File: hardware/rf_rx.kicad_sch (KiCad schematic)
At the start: 31 parts, among them J4 CON-SMA-EDGE-S, Q1 BC847C,215, U6 TL974IDR, U7 MAX4003

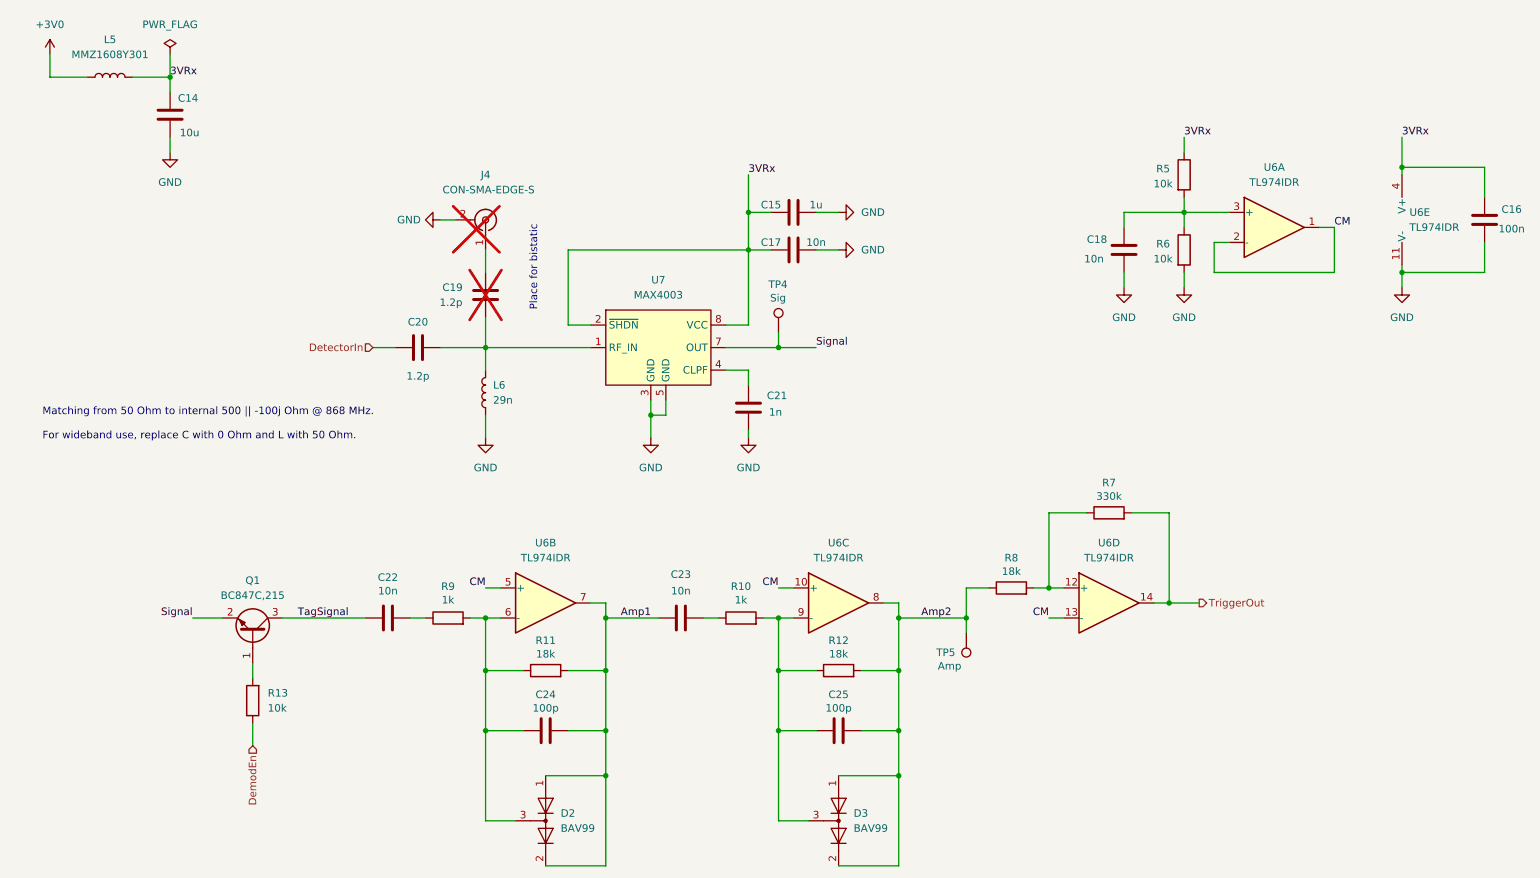
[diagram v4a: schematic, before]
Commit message: Rev 3. Back to transistor-based design since op-amp approach did not work well. Using UART bridge from other brand as FTDI was sold out.
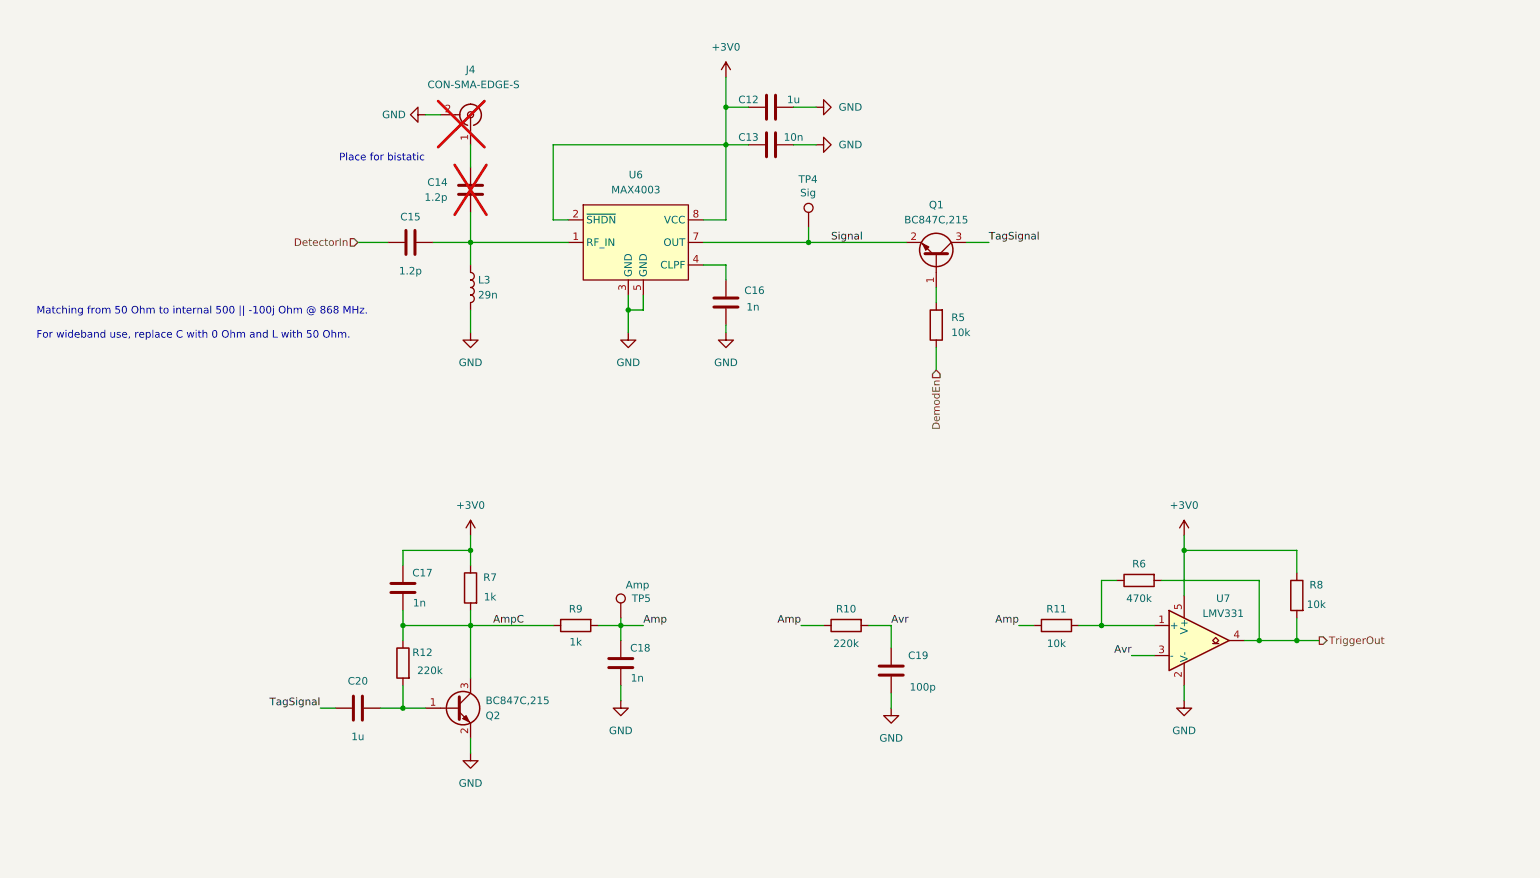
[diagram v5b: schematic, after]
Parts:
- removed C14: 10u, Capacitor_SMD:C_0603_1608Metric, symbol Device:C
- removed C16: 100n, Capacitor_SMD:C_0603_1608Metric, symbol Device:C
- removed C22, C23: 10n, Capacitor_SMD:C_0603_1608Metric, symbol Device:C
- removed C24, C25: 100p, Capacitor_SMD:C_0603_1608Metric, symbol Device:C
- removed D2, D3: BAV99, Package_TO_SOT_SMD:SOT-323_SC-70, symbol Diode:BAV99
- removed L5: MMZ1608Y301, Inductor_SMD:L_0603_1608Metric, symbol Device:L
- removed L6: 29n, Inductor_SMD:L_0603_1608Metric, symbol Device:L
- removed R5: 10k, Resistor_SMD:R_0603_1608Metric, symbol Device:R
- removed U6: TL974IDR, Package_SO:TSSOP-14_4.4x5mm_P0.65mm, symbol Amplifier_Operational:LM324
- added C17: 1n, Capacitor_SMD:C_0603_1608Metric, symbol Device:C
- added C19: 100p, Capacitor_SMD:C_0603_1608Metric, symbol Device:C
- added C20: 1u, Capacitor_SMD:C_0603_1608Metric, symbol Device:C
- added L3: 29n, Inductor_SMD:L_0603_1608Metric, symbol Device:L
- added Q2: BC847C,215, Package_TO_SOT_SMD:SOT-23, symbol Transistor_BJT:BC847
- added U7: LMV331, Package_TO_SOT_SMD:SOT-353_SC-70-5, symbol Comparator:LMV331
- C18: value 10n -> 1n
- R10: value 1k -> 220k
- R11, R8: value 18k -> 10k
- R12: value 18k -> 220k
- R6: value 10k -> 470k
- R7: value 330k -> 1k
- renumbered C15 to C12, C17 to C13, C19 to C14, C20 to C15, C21 to C16, R13 to R5, U7 to U6
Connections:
- net 3VRx is gone; now on net +3V0: C12.2, C13.2, U6.2 (~{SHDN}), U6.8 (VCC)
- net Amp1 is gone; now on an unnamed net: R11.2
- net +3V0: now also R7.1, R8.1, C17.1, U7.5 (V+)
- net GND: now also C18.2, C19.2, L3.2, Q2.2 (E), U7.2 (V-); no longer C18.1, R6.2
- net TagSignal: now also C20.1
- net TriggerOut: now also R6.2, R8.2, U7.4; no longer R7.2
- net Amp: now reaches R11.1, R9.2
- net Amp: now also C18.1, R10.1, TP5.1
- net AmpC: now reaches R12.1
- net AmpC: now also R7.2, R9.1, C17.2, Q2.3 (C); no longer R10.2
- net at R6.1: now also U7.1 (+); no longer C18.2
- net at C14.2, C15.1, U6.1 (RF_IN): now also L3.1
- removed net Amp2: R12.2, R8.1, TP5.1
- new net: C20.2, Q2.1 (B), R12.2
- new net Avr: C19.1, R10.2, U7.3 (-)
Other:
- moved on the sheet: C12, C13, C14, C15, C16, J4, Q1, R5, TP4, TP5, U6

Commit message: Rev 4. Removed coupler and detector IC. Using simple diode as detector.
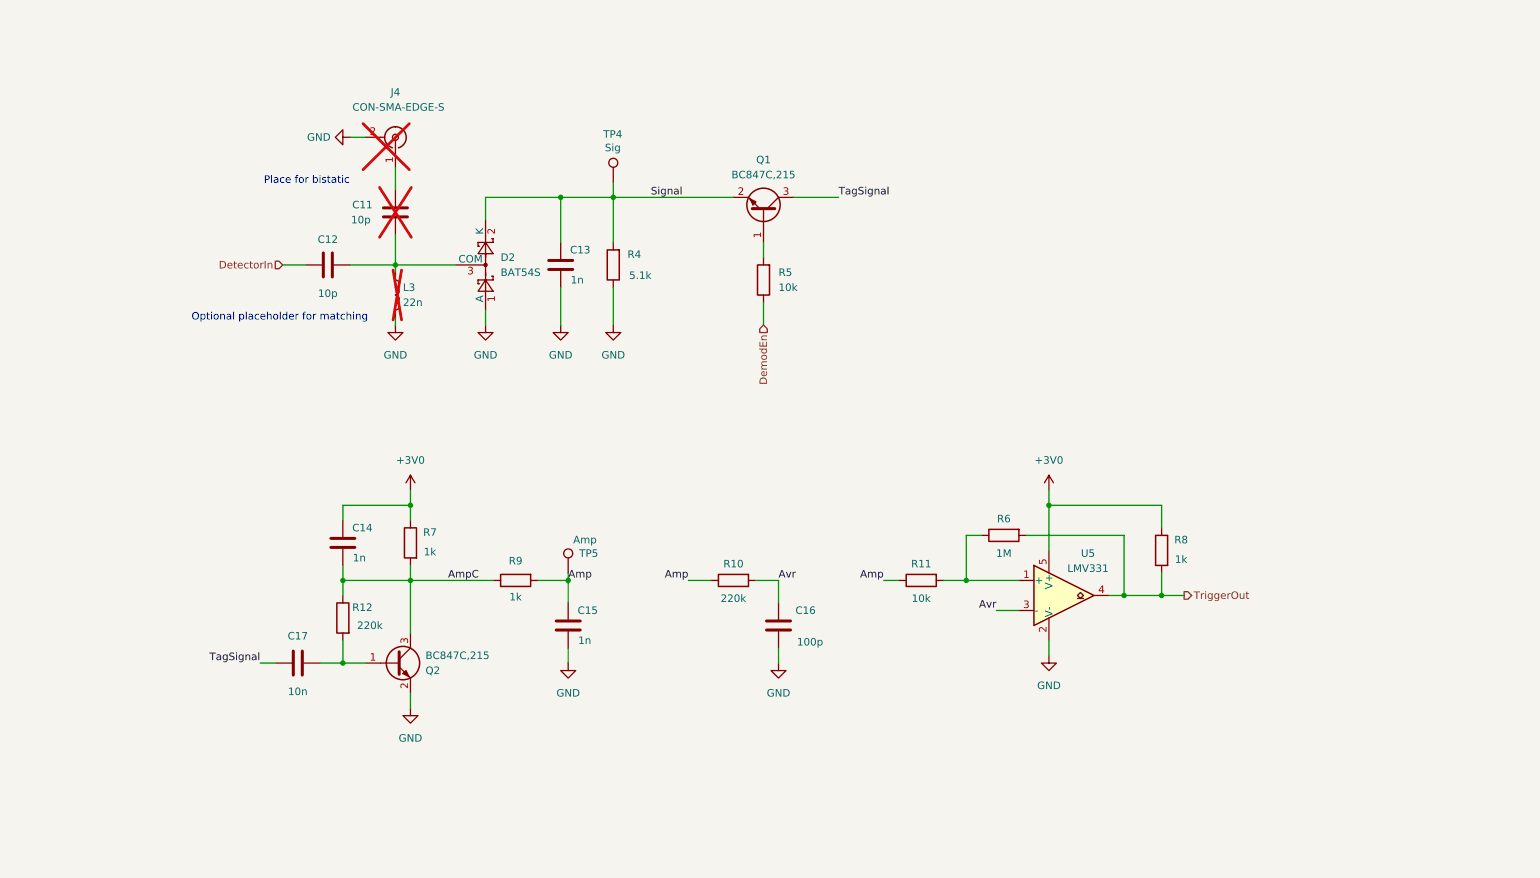
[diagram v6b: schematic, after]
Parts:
- removed C12: 1u, Capacitor_SMD:C_0603_1608Metric, symbol Device:C
- removed C13: 10n, Capacitor_SMD:C_0603_1608Metric, symbol Device:C
- removed U6: MAX4003, Package_SO:MSOP-8_3x3mm_P0.65mm, symbol ProjLib:MAX4003
- added D2: BAT54S, Package_TO_SOT_SMD:SOT-23, symbol Diode:BAT54S
- added R4: 5.1k, Resistor_SMD:R_0603_1608Metric, symbol Device:R
- C11: renamed from C14; value 1.2p -> 10p
- C12: renamed from C15; value 1.2p -> 10p
- C17: renamed from C20; value 1u -> 10n
- L3: value 29n -> 22n; now not fitted; now left out of the parts list
- R6: value 470k -> 1M
- R8: value 10k -> 1k
- renumbered C16 to C13, C17 to C14, C18 to C15, C19 to C16, U7 to U5
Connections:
- net GND: now also D2.1 (A), R4.1
- net Signal: now also C13.1, D2.2 (K), R4.2
- net at C11.2, C12.1, L3.1: now also D2.3 (COM)
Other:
- note added: "Optional placeholder for matching"
- note removed: "Matching from 50 Ohm to internal 500 || -100j Ohm @ 868 MHz. For wideband use, replace C with 0 Ohm and L with 50 Ohm."
- moved on the sheet: C11, C12, C13, C14, C15, C16, C17, J4, Q1, Q2, R10, R11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

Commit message: C12 is now 2.7pF to solve issue with too high detector voltage and reduce BOM
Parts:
- C12: value 10p -> 2.7p
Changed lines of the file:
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@@
 			)
 		)
-		(property "Value" "10p"
+		(property "Value" "2.7p"
 			(at 71.12 69.596 90)
 			(effects

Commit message: Fixed connector pinout according to silkscreen
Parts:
- R13: renamed from L3; value 22n -> 50R; footprint Inductor_SMD:L_0603_1608Metric -> Resistor_SMD:R_0603_1608Metric; symbol Device:L -> Device:R; now in the parts list
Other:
- note added: "BAT68-04 might be better"
